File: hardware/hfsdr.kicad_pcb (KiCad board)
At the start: 4 copper layers, 100 x 76 mm, 85 parts, among them J1 USB_C_Receptacle_USB2.0_16P, J4 JST PH S2B, Q1 AO3401A, SW1 RST, SW2 BOOT0, SW8 SW_SPDT, U1 SN74CBT3253, U2 XLV320ADC6120IRTER, U3 CH32V30xRxTx, U4 MD57E33QA3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

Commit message: feat: routing
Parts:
- added D2: LED, LED_SMD:LED_0805_2012Metric, F.Cu at (77.4, 87.9)
- moved C22 91.8 mm to (147.2, 50.0), turned to -90 degrees
- moved C8 74.9 mm to (119.2, 58.7)
- moved C9 65.1 mm to (127.4, 62.9), turned to -90 degrees
- moved C10 63.4 mm to (103.9, 60.8)
- moved H1 39.9 mm to (149.9, 101.2)
- moved C4 38.8 mm to (124.1, 62.7), turned to -45 degrees
- moved FB1 36.7 mm to (123.7, 74.2), turned to 45 degrees
- moved C39 32.2 mm to (152.5, 79.1), turned to 90 degrees
- moved FB4 31.6 mm to (154.5, 79.1), turned to 90 degrees
- moved C5 30.3 mm to (105.3, 64.2), turned to 45 degrees
- moved C11 30.0 mm to (122.2, 72.7), turned to -135 degrees
- moved SW8 29.2 mm to (91.6, 98.9)
- moved C41 26.8 mm to (152.5, 75.1), turned to -90 degrees
- moved C40 26.0 mm to (154.7, 75.2), turned to -90 degrees
- moved U4 19.7 mm to (103.1, 99.7)
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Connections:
- net DM renamed DN
- SW8 pad 1: unconnected-(SW8-A-Pad1) -> Net-(D1-K)
- SW8 pad 3: Net-(D1-K) -> unconnected-(SW8-C-Pad3)
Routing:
- net DP: track 3.75 -> 83.0 mm
- net DN: track 4.76 -> 82.4 mm
- net VBUS: track 9.85 -> 45.4 mm, vias 0 -> 2
- net GND: track 7.26 -> 42.8 mm, vias 1 -> 3
- net +3.3V: track 1.78 -> 36.8 mm, vias 0 -> 5
- net SCL: track 14.5 -> 34.8 mm
- net Net-(U1-VCC): track 0.00 -> 20.1 mm, vias 0 -> 2
- net SDA: track 14.9 -> 34.7 mm
- net Net-(D2-K): track 0.00 -> 13.2 mm
- net MCK: track 22.3 -> 34.6 mm
- net WS: track 20.3 -> 31.9 mm
- net CK: track 23.2 -> 34.1 mm
- net SD: track 25.5 -> 36.4 mm
- net +BATT: track 0.00 -> 9.71 mm
- net +5V: track 4.43 -> 14.0 mm
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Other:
- outline, holes or cut-outs redrawn

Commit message: feat: outline
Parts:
- added G***: LOGO, LOGO, B.Cu at (107.9, 67.1)
- moved G*** 131.7 mm to (231.8, 110.8)
- moved H1 93.6 mm to (73.3, 47.3)
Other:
- board size 100 x 76 mm -> 100.8 x 73.8 mm

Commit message: feat: finally got art in
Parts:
- removed the G*** at (107.9, 67.1)
- removed the G*** at (231.8, 110.8)
- added G***: LOGO, LOGO, B.Cu at (107.7, 67.2)
- moved RF1 3.06 mm to (147.0, 42.6)
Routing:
- net Net-(C29-Pad2): track 4.30 -> 0.00 mm
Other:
- outline, holes or cut-outs redrawn
- board text added: "BOOT"
- board text added: "RST"

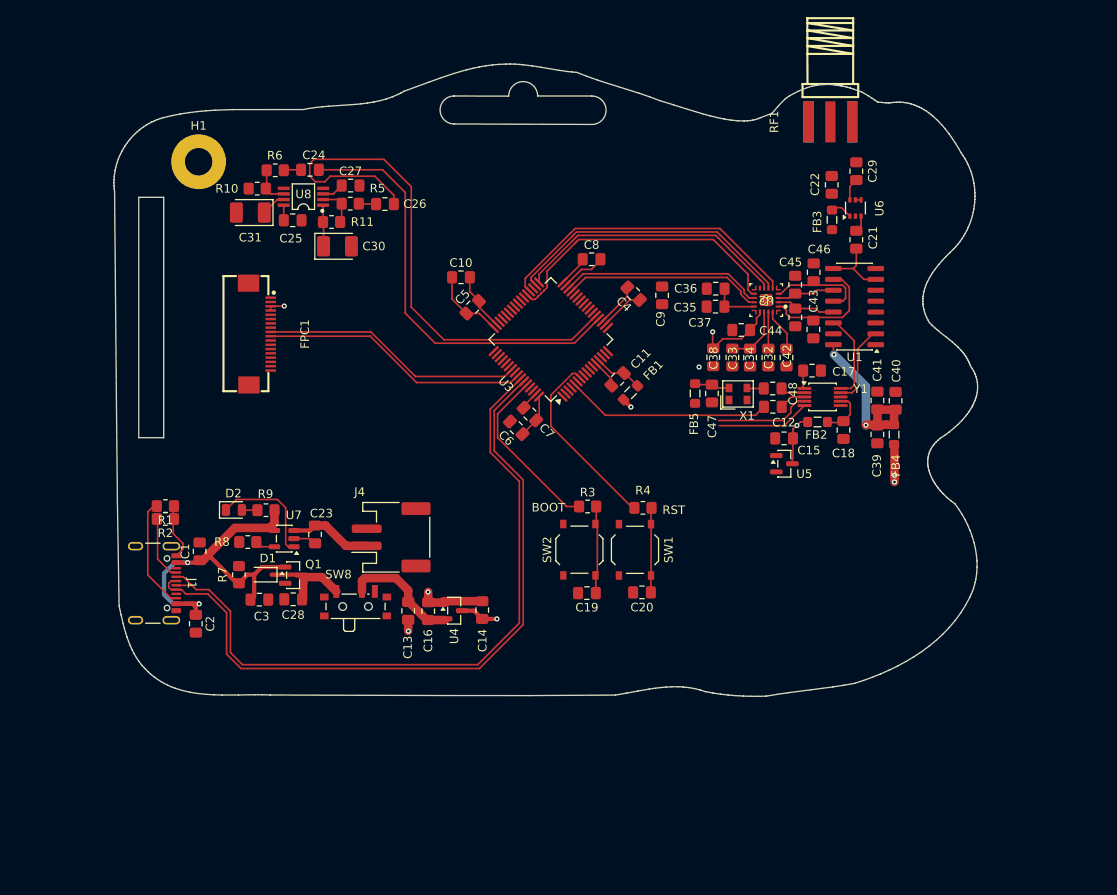
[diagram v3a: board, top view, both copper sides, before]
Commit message: feat: component adjustment position
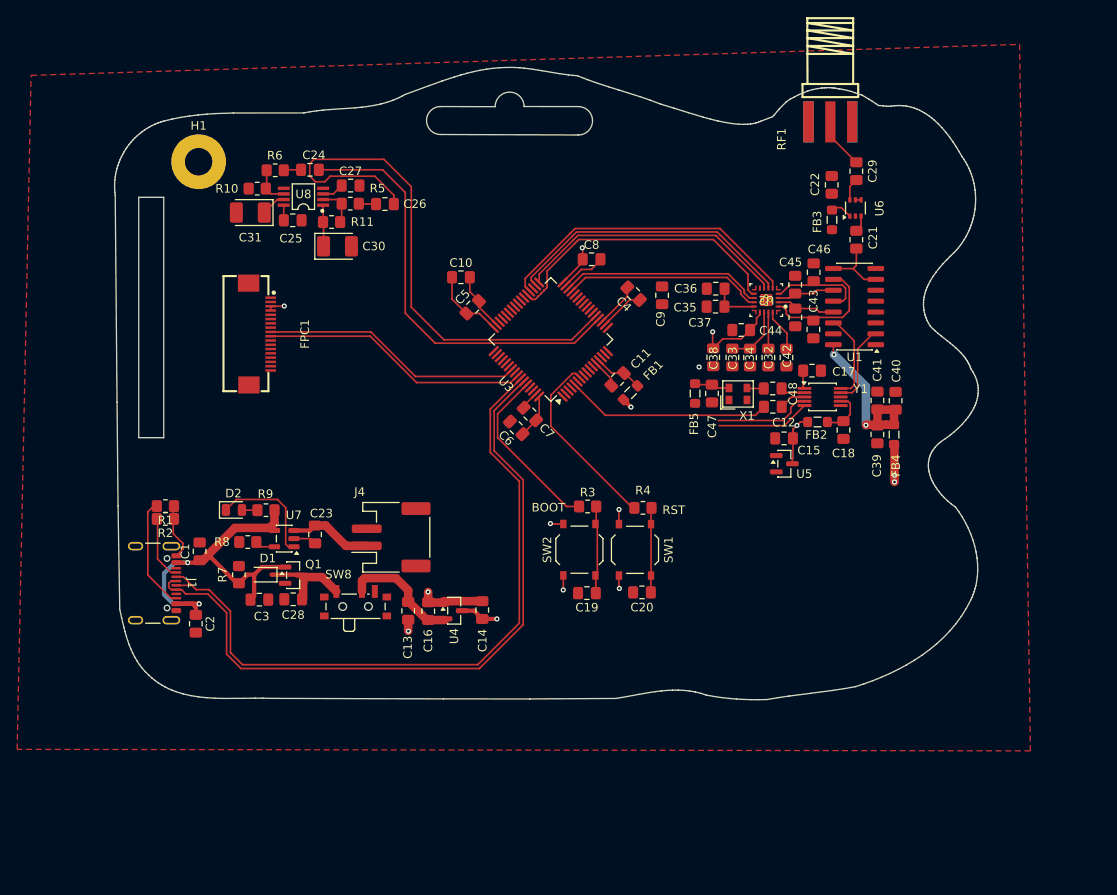
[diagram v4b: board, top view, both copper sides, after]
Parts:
- moved G*** 0.60 mm to (107.7, 67.8)
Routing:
- net +3.3V: track 36.8 -> 44.6 mm, vias 5 -> 10
- net Net-(C29-Pad2): track 0.00 -> 5.97 mm
- added copper zone on F.Cu, net GND
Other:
- outline, holes or cut-outs redrawn

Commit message: feat: rough routing and features
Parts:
- added J2: AudioPlug4, Connector_Audio:Jack_3.5mm_KoreanHropartsElec_PJ-320D-4A_Horizontal, F.Cu at (74.9, 50.1)
- moved H1 102.6 mm to (175.3, 58.7)
- moved C6 7.91 mm to (118.2, 77.1), turned to -45 degrees
- moved C26 4.32 mm to (99.2, 50.9)
- moved C27 4.32 mm to (95.2, 48.8)
- moved R11 4.32 mm to (93.0, 53.0)
- moved R5 4.32 mm to (95.1, 50.9)
- moved C24 4.32 mm to (90.4, 47.0)
- moved C25 4.32 mm to (88.4, 52.8)
- moved C30 4.32 mm to (93.7, 55.9)
- moved U8 4.32 mm to (89.7, 50.1)
- moved C31 4.32 mm to (83.5, 51.9)
- moved R10 4.32 mm to (84.3, 49.1)
- moved R6 4.32 mm to (86.4, 47.0)
- moved R1 0.56 mm to (69.5, 86.9), turned to 0 degrees
- moved D1 0.22 mm to (80.6, 95.4)
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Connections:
- C30 pad 2: unconnected-(C30-Pad2) -> Net-(C30-Pad2)
- C31 pad 2: unconnected-(C31-Pad2) -> Net-(C31-Pad2)
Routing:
- net +5V: track 14.0 -> 70.1 mm, vias 0 -> 4
- net GND: track 42.8 -> 76.5 mm, vias 3 -> 17
- net SDA: track 34.7 -> 60.3 mm, vias 0 -> 2
- net SCL: track 34.8 -> 59.9 mm, vias 0 -> 2
- net Net-(C30-Pad2): track 0.00 -> 19.2 mm
- net Net-(U1-VCC): track 20.1 -> 35.1 mm, vias 2 -> 3
- net +3.3VA: track 16.1 -> 27.6 mm, vias 2 -> 3
- net +3.3V: track 44.6 -> 54.3 mm, vias 10 -> 15
- net unconnected-(J4-MountPin-PadMP): track 0.00 -> 6.70 mm
- net +BATT: track 9.71 -> 15.5 mm
- net Net-(C31-Pad2): track 0.00 -> 4.55 mm
- net Net-(U8-V02): track 2.90 -> 6.45 mm
- net DAC1_OUT: track 50.5 -> 47.3 mm
- net DAC2_OUT: track 65.5 -> 62.7 mm
- net Net-(D1-K): track 10.8 -> 12.3 mm
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
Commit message: feat: most rules fixed?
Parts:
- removed H1: MountingHole_Pad, MountingHole:MountingHole_3.2mm_M3_Pad
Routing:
- net GND: track 76.5 -> 80.0 mm
- net VBUS: track 46.5 -> 47.9 mm
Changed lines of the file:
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@@
 	(net 116 "unconnected-(FPC1-Pad19)")
 	(net 117 "Net-(D1-K)")
-	(net 118 "unconnected-(H1-Pad1)")
-	(net 119 "unconnected-(J1-SHIELD-PadS1)_1")
-	(net 120 "unconnected-(J1-SHIELD-PadS1)_2")
-	(net 121 "unconnected-(J1-SHIELD-PadS1)_3")
-	(net 122 "unconnected-(J4-MountPin-PadMP)")
-	(net 123 "unconnected-(SW8-C-Pad3)")
-	(net 124 "SWDIO")
-	(net 125 "SWCLK")
-	(net 126 "DN")
-	(net 127 "unconnected-(J2-PadS)")
+	(net 118 "unconnected-(J1-SHIELD-PadS1)_1")
+	(net 119 "unconnected-(J1-SHIELD-PadS1)_2")
+	(net 120 "unconnected-(J1-SHIELD-PadS1)_3")
+	(net 121 "unconnected-(J4-MountPin-PadMP)")
+	(net 122 "unconnected-(SW8-C-Pad3)")
+	(net 123 "SWDIO")
+	(net 124 "SWCLK")
+	(net 125 "DN")
+	(net 126 "unconnected-(J2-PadS)")
 	(footprint "Capacitor_SMD:C_0805_2012Metric_Pad1.18x1.45mm_HandSolder"
 		(layer "F.Cu")
@@
 			(size 1.2 2.5)
 			(layers "F.Cu" "F.Mask" "F.Paste")
-			(net 127 "unconnected-(J2-PadS)")
+			(net 126 "unconnected-(J2-PadS)")
 			(pintype "passive")
 		)
@@
 			(size 0.7 1.5)
 			(layers "F.Cu" "F.Mask" "F.Paste")
-			(net 123 "unconnected-(SW8-C-Pad3)")
+			(net 122 "unconnected-(SW8-C-Pad3)")
 			(pinfunction "C")
 			(pintype "passive")
@@
 			(layers "F.Cu" "F.Mask" "F.Paste")
 			(roundrect_rratio 0.25)
-			(net 124 "SWDIO")
+			(net 123 "SWDIO")
 			(pinfunction "SWDIO")
 			(pintype "bidirectional")
@@
 			(layers "F.Cu" "F.Mask" "F.Paste")
 			(roundrect_rratio 0.25)
-			(net 125 "SWCLK")
+			(net 124 "SWCLK")
 			(pinfunction "SWCLK")
 			(pintype "bidirectional")
@@
 			(layers "F.Cu" "F.Mask" "F.Paste")
 			(roundrect_rratio 0.25)
-			(net 126 "DN")
+			(net 125 "DN")
 			(pinfunction "PB6")
 			(pintype "bidirectional")
@@
 			(layers "F.Cu" "F.Mask" "F.Paste")
 			(roundrect_rratio 0.166667)
-			(net 122 "unconnected-(J4-MountPin-PadMP)")
+			(net 121 "unconnected-(J4-MountPin-PadMP)")
 			(pinfunction "MountPin")
 			(pintype "passive")
@@
 			(layers "F.Cu" "F.Mask" "F.Paste")
 			(roundrect_rratio 0.166667)
-			(net 122 "unconnected-(J4-MountPin-PadMP)")
+			(net 121 "unconnected-(J4-MountPin-PadMP)")
 			(pinfunction "MountPin")
 			(pintype "passive")
@@
 			(layers "F.Cu" "F.Mask" "F.Paste")
 			(roundrect_rratio 0.25)
-			(net 126 "DN")
+			(net 125 "DN")
 			(pinfunction "D-")
 			(pintype "bidirectional")
@@
 			(layers "F.Cu" "F.Mask" "F.Paste")
 			(roundrect_rratio 0.25)
-			(net 126 "DN")
+			(net 125 "DN")
 			(pinfunction "D-")
 			(pintype "bidirectional")
@@
 			(layers "*.Cu" "*.Mask" "F.Paste")
 			(remove_unused_layers no)
-			(net 119 "unconnected-(J1-SHIELD-PadS1)_1")
+			(net 118 "unconnected-(J1-SHIELD-PadS1)_1")
 			(pinfunction "SHIELD")
 			(pintype "passive+no_connect")
@@
 			(layers "*.Cu" "*.Mask" "F.Paste")
 			(remove_unused_layers no)
-			(net 120 "unconnected-(J1-SHIELD-PadS1)_2")
+			(net 119 "unconnected-(J1-SHIELD-PadS1)_2")
 			(pinfunction "SHIELD")
 			(pintype "passive+no_connect")
@@
 			(layers "*.Cu" "*.Mask" "F.Paste")
 			(remove_unused_layers no)
-			(net 121 "unconnected-(J1-SHIELD-PadS1)_3")
+			(net 120 "unconnected-(J1-SHIELD-PadS1)_3")
 			(pinfunction "SHIELD")
 			(pintype "passive+no_connect")
@@
 		)
 	)
-	(footprint "MountingHole:MountingHole_3.2mm_M3_Pad"
-		(layer "F.Cu")
-		(at 175.307547 58.678206)
-		(descr "Mounting Hole 3.2mm, M3")
-		(tags "mounting hole 3.2mm m3")
-		(property "Reference" "H1"
-			(at 0 -4.2 0)
-			(layer "F.SilkS")
-			(effects
-				(font
-					(size 1 1)
-					(thickness 0.15)
-				)
-			)
-		)
-		(property "Value" "MountingHole_Pad"
-			(at 0 4.2 0)
-			(layer "F.Fab")
-			(effects
-				(font
-					(size 1 1)
-					(thickness 0.15)
-				)
-			)
-		)
-		(property "Datasheet" ""
-			(at 0 0 0)
-			(unlocked yes)
-			(layer "F.Fab")
-			(hide yes)
-			(effects
-				(font
-					(size 1.27 1.27)
-					(thickness 0.15)
-				)
-			)
-		)
-		(property "Description" "Mounting Hole with connection"
-			(at 0 0 0)
-			(unlocked yes)
-			(layer "F.Fab")
-			(hide yes)
-			(effects
-				(font
-					(size 1.27 1.27)
-					(thickness 0.15)
-				)
-			)
-		)
-		(property ki_fp_filters "MountingHole*Pad*")
-		(sheetname "/")
-		(sheetfile "hfsdr.kicad_sch")
-		(attr exclude_from_pos_files exclude_from_bom)
-		(fp_circle
-			(center 0 0)
-			(end 3.2 0)
-			(stroke
-				(width 0.15)
-				(type solid)
-			)
-			(fill no)
-			(layer "Cmts.User")
-		)
-		(fp_circle
-			(center 0 0)
-			(end 3.45 0)
-			(stroke
-				(width 0.05)
-				(type solid)
-			)
-			(fill no)
-			(layer "F.CrtYd")
-		)
-		(fp_text user "${REFERENCE}"
-			(at 0 0 0)
-			(layer "F.Fab")
-			(effects
-				(font
-					(size 1 1)
-					(thickness 0.15)
-				)
-			)
-		)
-		(pad "1" thru_hole circle
-			(at 0 0)
-			(size 6.4 6.4)
-			(drill 3.2)
-			(layers "*.Cu" "*.Mask")
-			(remove_unused_layers no)
-			(net 118 "unconnected-(H1-Pad1)")
-			(pinfunction "1")
-			(pintype "input")
-		)
-		(embedded_fonts no)
-	)
 	(footprint "Capacitor_SMD:C_0805_2012Metric_Pad1.18x1.45mm_HandSolder"
 		(layer "F.Cu")
@@
 	)
 	(segment
+		(start 70.698475 99.664118)
+		(end 72.983423 101.949066)
+		(width 0.2)
+		(layer "F.Cu")
+		(net 13)
+	)
+	(segment
 		(start 86.59667 93.421808)
 		(end 84.667682 93.421808)
@@
 	)
 	(segment
+		(start 72.983423 101.949066)
+		(end 72.983423 102.232575)
+		(width 0.2)
+		(layer "F.Cu")
+		(net 13)
+	)
+	(segment
 		(start 81.719296 63.134186)
 		(end 80.842296 63.134186)
@@
 	)
 	(segment
-		(start 72.033839 94.064118)
-		(end 70.698475 94.064118)
+		(start 73.37162 99.769378)
+		(end 73.37162 98.876106)
 		(width 0.5)
 		(layer "F.Cu")
@@
 	)
 	(segment
-		(start 72.593724 98.876106)
-		(end 72.983423 99.265805)
+		(start 72.033839 94.064118)
+		(end 70.698475 94.064118)
 		(width 0.5)
 		(layer "F.Cu")
@@
 	)
 	(segment
+		(start 72.983423 99.264303)
+		(end 72.983423 100.157575)
+		(width 0.5)
+		(layer "F.Cu")
+		(net 80)
+	)
+	(segment
 		(start 73.836813 93.783007)
 		(end 73.42556 93.783007)
@@
 	)
 	(segment
+		(start 73.37162 98.876106)
+		(end 72.983423 99.264303)
+		(width 0.5)
+		(layer "F.Cu")
+		(net 80)
+	)
+	(segment
 		(start 82.736325 90.311071)
 		(end 82.159556 90.311071)
@@
 	)
 	(segment
-		(start 79.791537 95.464442)
-		(end 79.791537 97.952524)
+		(start 72.983423 100.157575)
+		(end 73.37162 99.769378)
 		(width 0.5)
 		(layer "F.Cu")
@@
 	)
 	(segment
-		(start 72.983423 99.265805)
-		(end 72.983423 100.157575)
+		(start 79.791537 95.464442)
+		(end 79.791537 97.952524)
 		(width 0.5)
 		(layer "F.Cu")
@@
 		(width 0.2)
 		(layer "F.Cu")
-		(net 122)
+		(net 121)
 	)
 	(segment
@@
 		(width 0.2)
 		(layer "F.Cu")
-		(net 126)
+		(net 125)
 	)
 	(segment
@@
 		(width 0.2)
 		(layer "F.Cu")
-		(net 126)
+		(net 125)
 	)
 	(segment
@@
 		(width 0.2)
 		(layer "F.Cu")
-		(net 126)
+		(net 125)
 	)
 	(segment
@@
 		(width 0.2)
 		(layer "F.Cu")
-		(net 126)
+		(net 125)
 	)
 	(segment
@@
 		(width 0.2)
 		(layer "F.Cu")
-		(net 126)
+		(net 125)
 	)
 	(segment
@@
 		(width 0.2)
 		(layer "F.Cu")
-		(net 126)
+		(net 125)
 	)
 	(segment
@@
 		(width 0.2)
 		(layer "F.Cu")
-		(net 126)
+		(net 125)
 	)
 	(segment
@@
 		(width 0.2)
 		(layer "F.Cu")
-		(net 126)
+		(net 125)
 	)
 	(segment
@@
 		(width 0.2)
 		(layer "F.Cu")
-		(net 126)
+		(net 125)
 	)
 	(segment
@@
 		(width 0.2)
 		(layer "F.Cu")
-		(net 126)
+		(net 125)
 	)
 	(segment
@@
 		(width 0.2)
 		(layer "F.Cu")
-		(net 126)
+		(net 125)
 	)
 	(segment
@@
 		(width 0.2)
 		(layer "F.Cu")
-		(net 126)
+		(net 125)
 	)
 	(segment
@@
 		(width 0.2)
 		(layer "F.Cu")
-		(net 126)
+		(net 125)
 	)
 	(segment
@@
 		(width 0.2)
 		(layer "F.Cu")
-		(net 126)
+		(net 125)
 	)
 	(zone

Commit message: feat: credits
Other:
- board text added: "github.com/rhgndf/hfsdr rhgndf & hackin7"
- board text added: "hfsdr"
